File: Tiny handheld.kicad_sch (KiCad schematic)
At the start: 39 parts, among them IC1 BQ21040DBVR, J1 VDisplay/prog1, J2 HDisplay/prog, J3 USB_C_Receptacle_USB2.0, U1 ATtiny85-20P, U2 ATtiny85-20S

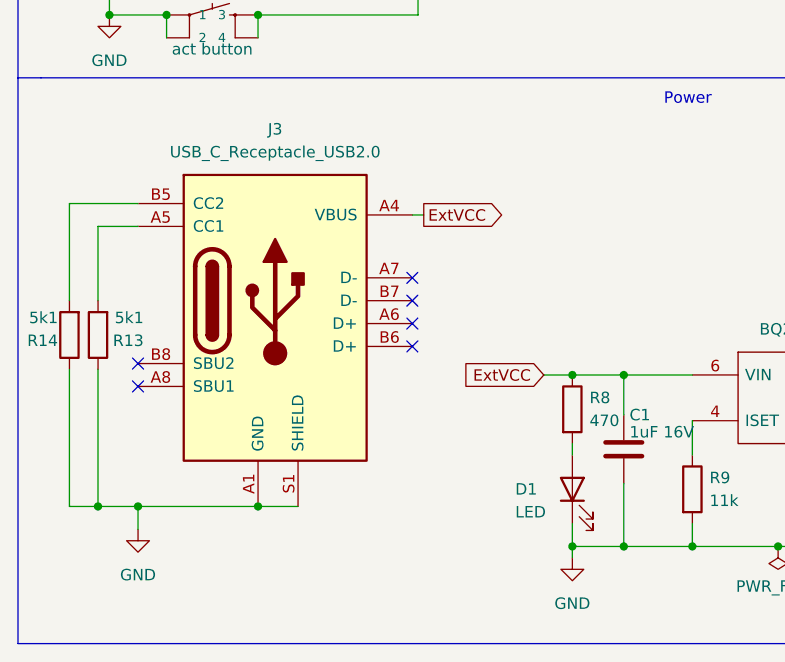
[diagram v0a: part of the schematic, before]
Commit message: added power testpoints
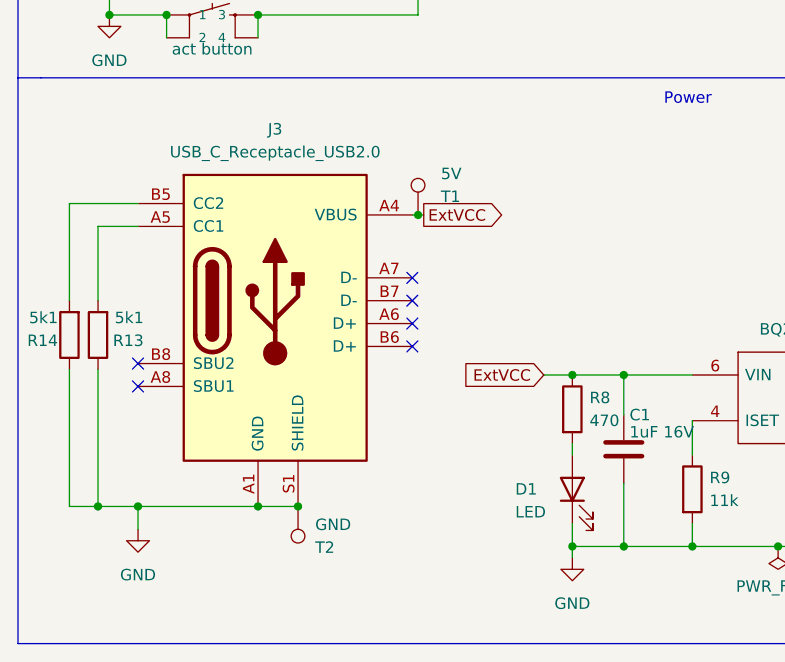
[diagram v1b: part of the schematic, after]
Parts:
- added 5V: T1, TestPoint:TestPoint_Pad_1.0x1.0mm, symbol Connector:TestPoint
- added GND: T2, TestPoint:TestPoint_Pad_1.0x1.0mm, symbol Connector:TestPoint
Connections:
- net ExtVCC: now also 5V.1
- net GND: now also GND.1
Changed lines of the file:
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@@
   (junction (at 117.475 133.985) (diameter 0) (color 0 0 0 0)
   )
+  (junction (at 43.815 137.16) (diameter 0) (color 0 0 0 0)
+  )
   (junction (at 107.315 141.605) (diameter 0) (color 0 0 0 0)
   )
@@
   )
   (junction (at 165.1 29.845) (diameter 0) (color 0 0 0 0)
+  )
+  (junction (at 57.15 104.775) (diameter 0) (color 0 0 0 0)
   )
   (junction (at 241.3 72.39) (diameter 0) (color 0 0 0 0)
@@
     (stroke (width 0) (type default) (color 0 0 0 0))
   )
-  (wire (pts (xy 56.515 104.775) (xy 57.785 104.775))
+  (wire (pts (xy 56.515 104.775) (xy 57.15 104.775))
     (stroke (width 0) (type default) (color 0 0 0 0))
   )
@@
   )
   (wire (pts (xy 165.1 29.845) (xy 177.8 29.845))
+    (stroke (width 0) (type default) (color 0 0 0 0))
+  )
+  (wire (pts (xy 57.15 104.775) (xy 57.785 104.775))
     (stroke (width 0) (type default) (color 0 0 0 0))
   )
@@
     (pin "2")
   )
+  (symbol (lib_id "Connector:TestPoint") (at 57.15 104.775 0) (unit 1)
+    (in_bom yes) (on_board yes) (fields_autoplaced)
+    (property "Reference" "5V" (id 0) (at 59.69 100.2029 0)
+      (effects (font (size 1.27 1.27)) (justify left))
+    )
+    (property "Value" "T1" (id 1) (at 59.69 102.7429 0)
+      (effects (font (size 1.27 1.27)) (justify left))
+    )
+    (property "Footprint" "TestPoint:TestPoint_Pad_1.0x1.0mm" (id 2) (at 62.23 104.775 0)
+      (effects (font (size 1.27 1.27)) hide)
+    )
+    (property "Datasheet" "~" (id 3) (at 62.23 104.775 0)
+      (effects (font (size 1.27 1.27)) hide)
+    )
+    (pin "1")
+  )
   (symbol (lib_id "Device:LED") (at 74.295 135.255 90) (unit 1)
     (in_bom yes) (on_board yes)
@@
     (pin "5")
     (pin "6")
+  )
+  (symbol (lib_id "Connector:TestPoint") (at 43.815 137.16 180) (unit 1)
+    (in_bom yes) (on_board yes) (fields_autoplaced)
+    (property "Reference" "GND" (id 0) (at 45.72 139.1919 0)
+      (effects (font (size 1.27 1.27)) (justify right))
+    )
+    (property "Value" "T2" (id 1) (at 45.72 141.7319 0)
+      (effects (font (size 1.27 1.27)) (justify right))
+    )
+    (property "Footprint" "TestPoint:TestPoint_Pad_1.0x1.0mm" (id 2) (at 38.735 137.16 0)
+      (effects (font (size 1.27 1.27)) hide)
+    )
+    (property "Datasheet" "~" (id 3) (at 38.735 137.16 0)
+      (effects (font (size 1.27 1.27)) hide)
+    )
+    (pin "1")
   )
   (symbol (lib_id "Device:C") (at 150.495 60.325 0) (unit 1)
@@
       (reference "#PWR0114") (unit 1) (value "GNDPWR") (footprint "")
     )
+    (path "/340146ae-1dcd-4cc9-b1a4-794b73097a69"
+      (reference "5V") (unit 1) (value "T1") (footprint "TestPoint:TestPoint_Pad_1.0x1.0mm")
+    )
     (path "/d87d81d6-a9f7-455a-b1d8-8ff0988a0a64"
       (reference "BT1") (unit 1) (value "BATTERY-6.8MM_SMD") (footprint "Battery:BatteryHolder_Keystone_3002_1x2032")
@@
       (reference "D2") (unit 1) (value "LED") (footprint "LED_SMD:LED_1206_3216Metric_Pad1.42x1.75mm_HandSolder")
     )
+    (path "/42350c44-064d-4037-affd-69bc19043671"
+      (reference "GND") (unit 1) (value "T2") (footprint "TestPoint:TestPoint_Pad_1.0x1.0mm")
+    )
     (path "/a18d266d-c0d2-4b00-9a60-ec95f250657b"

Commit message: Start Routing
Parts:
- renumbered 5V to 5V1, GND to GND1
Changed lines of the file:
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@@
   (symbol (lib_id "Connector:TestPoint") (at 57.15 104.775 0) (unit 1)
     (in_bom yes) (on_board yes) (fields_autoplaced)
-    (property "Reference" "5V" (id 0) (at 59.69 100.2029 0)
+    (property "Reference" "5V1" (id 0) (at 59.69 100.2029 0)
       (effects (font (size 1.27 1.27)) (justify left))
     )
@@
   (symbol (lib_id "Connector:TestPoint") (at 43.815 137.16 180) (unit 1)
     (in_bom yes) (on_board yes) (fields_autoplaced)
-    (property "Reference" "GND" (id 0) (at 45.72 139.1919 0)
+    (property "Reference" "GND1" (id 0) (at 45.72 139.1919 0)
       (effects (font (size 1.27 1.27)) (justify right))
     )
@@
     )
     (path "/340146ae-1dcd-4cc9-b1a4-794b73097a69"
-      (reference "5V") (unit 1) (value "T1") (footprint "TestPoint:TestPoint_Pad_1.0x1.0mm")
+      (reference "5V1") (unit 1) (value "T1") (footprint "TestPoint:TestPoint_Pad_1.0x1.0mm")
     )
     (path "/d87d81d6-a9f7-455a-b1d8-8ff0988a0a64"
@@
     )
     (path "/42350c44-064d-4037-affd-69bc19043671"
-      (reference "GND") (unit 1) (value "T2") (footprint "TestPoint:TestPoint_Pad_1.0x1.0mm")
+      (reference "GND1") (unit 1) (value "T2") (footprint "TestPoint:TestPoint_Pad_1.0x1.0mm")
     )
     (path "/a18d266d-c0d2-4b00-9a60-ec95f250657b"

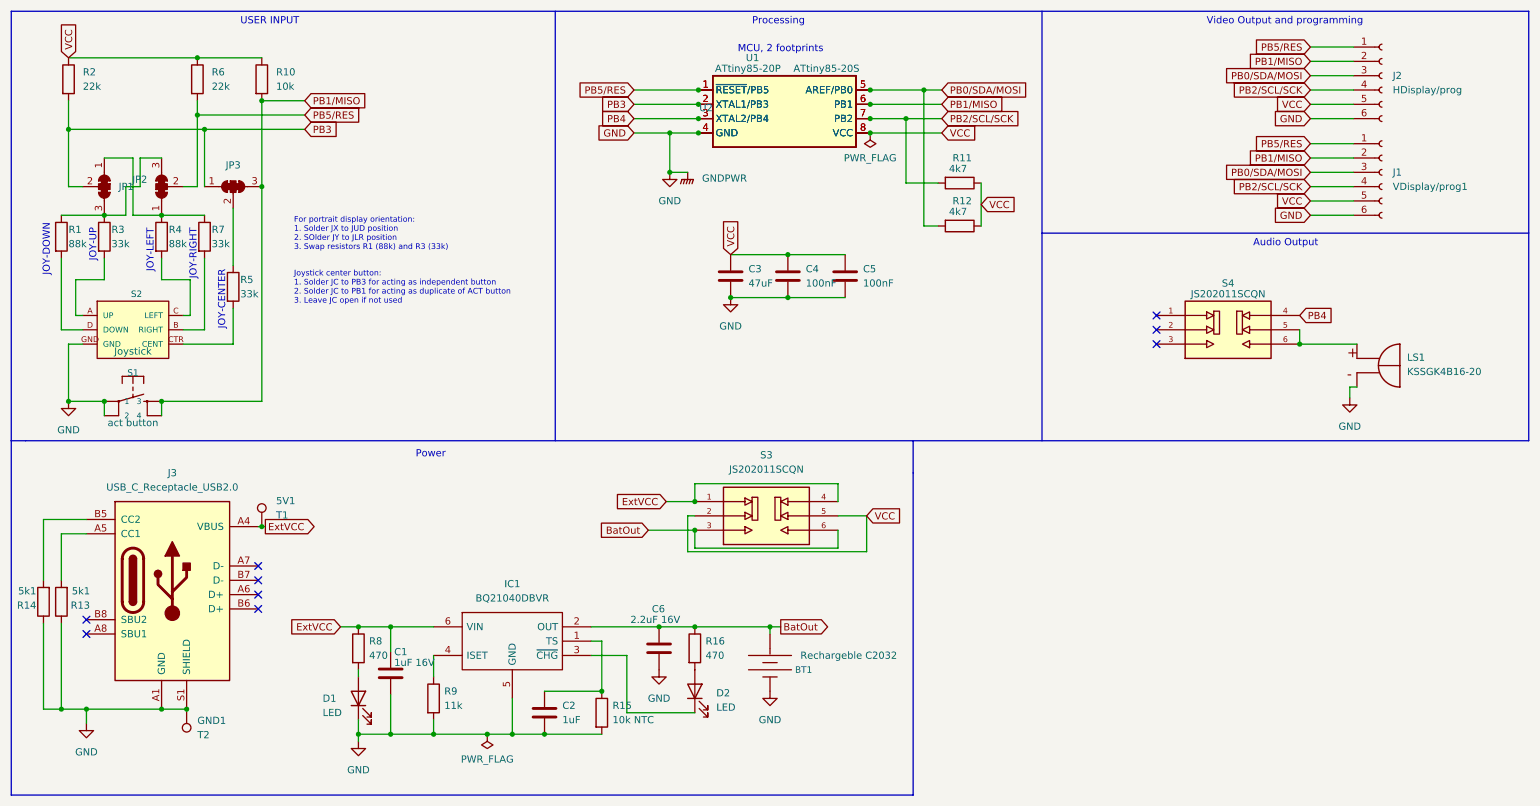
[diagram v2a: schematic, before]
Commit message: enh pcb layout and silkscreen
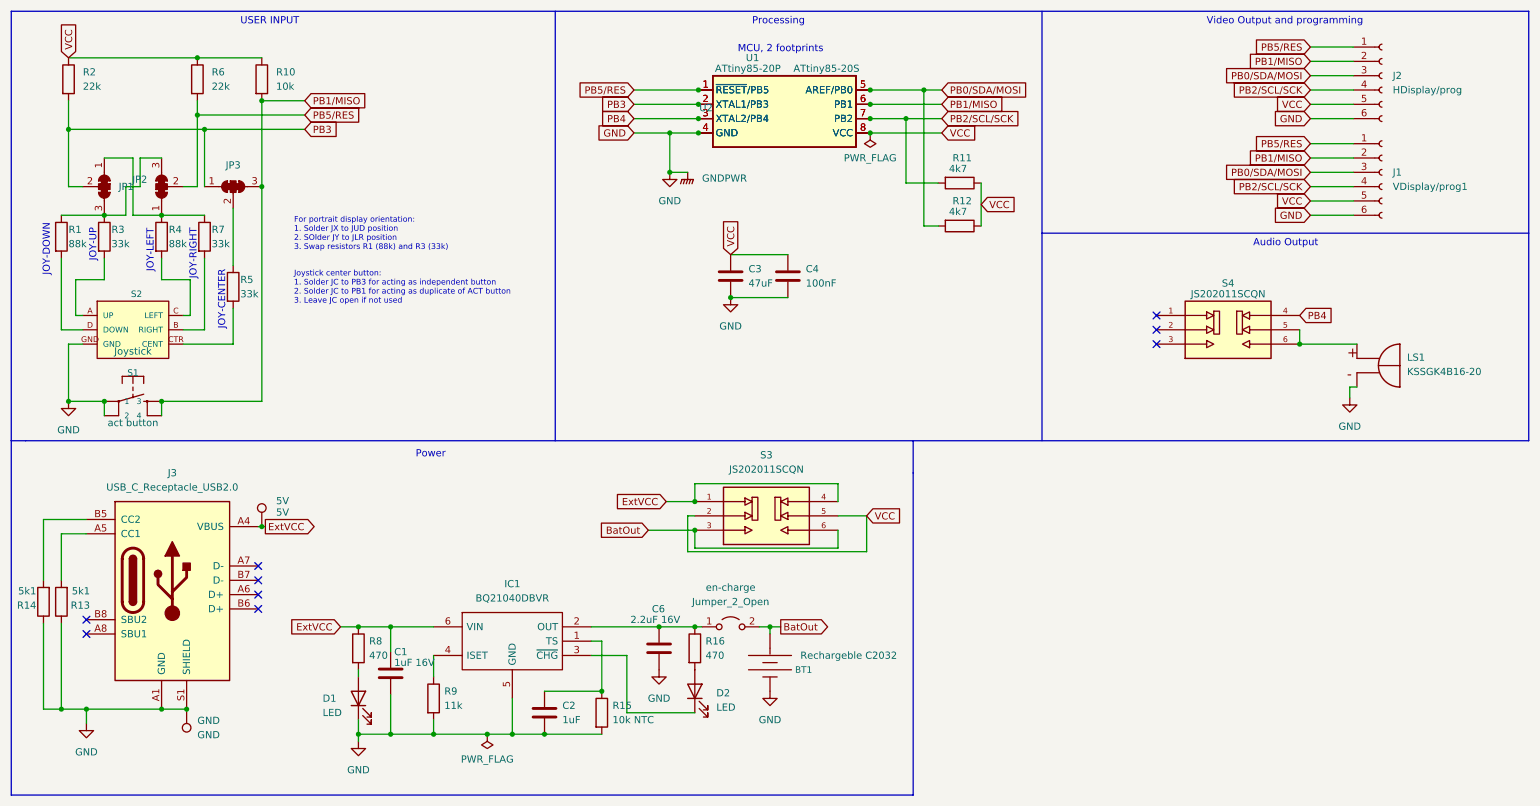
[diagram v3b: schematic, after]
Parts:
- removed C5: 100nF, Capacitor_SMD:C_1206_3216Metric_Pad1.33x1.80mm_HandSolder, symbol Device:C
- added en-charge: Jumper_2_Open, Jumper:SolderJumper-2_P1.3mm_Open_RoundedPad1.0x1.5mm, symbol Jumper:Jumper_2_Open
- 5V: renamed from 5V1; value T1 -> 5V
- GND: renamed from GND1; value T2 -> GND
- R15: Purpose Temperature sense resistor -> Battery temperature sense resistor
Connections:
- net BatOut: now also en-charge.2 (B); no longer C6.1, IC1.2 (OUT), R16.1
- new net: C6.1, IC1.2 (OUT), R16.1, en-charge.1 (A)
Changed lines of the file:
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@@
   (junction (at 80.01 122.555) (diameter 0) (color 0 0 0 0)
   )
+  (junction (at 134.62 32.385) (diameter 0) (color 0 0 0 0)
+  )
+  (junction (at 165.1 34.925) (diameter 0) (color 0 0 0 0)
+  )
+  (junction (at 165.1 32.385) (diameter 0) (color 0 0 0 0)
+  )
+  (junction (at 57.15 44.45) (diameter 0) (color 0 0 0 0)
+  )
+  (junction (at 57.15 29.21) (diameter 0) (color 0 0 0 0)
+  )
+  (junction (at 39.37 137.16) (diameter 0) (color 0 0 0 0)
+  )
+  (junction (at 97.155 141.605) (diameter 0) (color 0 0 0 0)
+  )
+  (junction (at 21.59 137.16) (diameter 0) (color 0 0 0 0)
+  )
+  (junction (at 133.985 100.33) (diameter 0) (color 0 0 0 0)
+  )
+  (junction (at 140.335 64.135) (diameter 0) (color 0 0 0 0)
+  )
+  (junction (at 45.72 21.59) (diameter 0) (color 0 0 0 0)
+  )
+  (junction (at 129.54 41.91) (diameter 0) (color 0 0 0 0)
+  )
+  (junction (at 74.295 141.605) (diameter 0) (color 0 0 0 0)
+  )
+  (junction (at 134.62 34.925) (diameter 0) (color 0 0 0 0)
+  )
+  (junction (at 26.035 137.16) (diameter 0) (color 0 0 0 0)
+  )
+  (junction (at 117.475 133.985) (diameter 0) (color 0 0 0 0)
+  )
+  (junction (at 43.815 137.16) (diameter 0) (color 0 0 0 0)
+  )
+  (junction (at 107.315 141.605) (diameter 0) (color 0 0 0 0)
+  )
+  (junction (at 74.295 122.555) (diameter 0) (color 0 0 0 0)
+  )
+  (junction (at 80.01 141.605) (diameter 0) (color 0 0 0 0)
+  )
+  (junction (at 134.62 27.305) (diameter 0) (color 0 0 0 0)
+  )
+  (junction (at 171.45 32.385) (diameter 0) (color 0 0 0 0)
+  )
+  (junction (at 101.6 141.605) (diameter 0) (color 0 0 0 0)
+  )
+  (junction (at 129.54 34.925) (diameter 0) (color 0 0 0 0)
+  )
   (junction (at 147.32 122.555) (diameter 0) (color 0 0 0 0)
   )
-  (junction (at 134.62 32.385) (diameter 0) (color 0 0 0 0)
-  )
-  (junction (at 165.1 34.925) (diameter 0) (color 0 0 0 0)
-  )
-  (junction (at 165.1 32.385) (diameter 0) (color 0 0 0 0)
-  )
-  (junction (at 57.15 44.45) (diameter 0) (color 0 0 0 0)
-  )
-  (junction (at 57.15 29.21) (diameter 0) (color 0 0 0 0)
-  )
-  (junction (at 39.37 137.16) (diameter 0) (color 0 0 0 0)
-  )
-  (junction (at 97.155 141.605) (diameter 0) (color 0 0 0 0)
-  )
-  (junction (at 21.59 137.16) (diameter 0) (color 0 0 0 0)
-  )
-  (junction (at 133.985 100.33) (diameter 0) (color 0 0 0 0)
-  )
-  (junction (at 140.335 64.135) (diameter 0) (color 0 0 0 0)
-  )
-  (junction (at 45.72 21.59) (diameter 0) (color 0 0 0 0)
-  )
-  (junction (at 129.54 41.91) (diameter 0) (color 0 0 0 0)
-  )
-  (junction (at 74.295 141.605) (diameter 0) (color 0 0 0 0)
-  )
-  (junction (at 134.62 34.925) (diameter 0) (color 0 0 0 0)
-  )
-  (junction (at 26.035 137.16) (diameter 0) (color 0 0 0 0)
-  )
-  (junction (at 117.475 133.985) (diameter 0) (color 0 0 0 0)
-  )
-  (junction (at 43.815 137.16) (diameter 0) (color 0 0 0 0)
-  )
-  (junction (at 107.315 141.605) (diameter 0) (color 0 0 0 0)
-  )
-  (junction (at 74.295 122.555) (diameter 0) (color 0 0 0 0)
-  )
-  (junction (at 80.01 141.605) (diameter 0) (color 0 0 0 0)
-  )
-  (junction (at 134.62 27.305) (diameter 0) (color 0 0 0 0)
-  )
-  (junction (at 171.45 32.385) (diameter 0) (color 0 0 0 0)
-  )
-  (junction (at 101.6 141.605) (diameter 0) (color 0 0 0 0)
-  )
-  (junction (at 129.54 34.925) (diameter 0) (color 0 0 0 0)
-  )
   (junction (at 87.63 141.605) (diameter 0) (color 0 0 0 0)
   )
-  (junction (at 150.495 64.135) (diameter 0) (color 0 0 0 0)
-  )
-  (junction (at 150.495 56.515) (diameter 0) (color 0 0 0 0)
-  )
   (junction (at 22.86 82.55) (diameter 0) (color 0 0 0 0)
   )
   (junction (at 29.21 49.53) (diameter 0) (color 0 0 0 0)
   )
+  (junction (at 46.99 34.29) (diameter 0) (color 0 0 0 0)
+  )
+  (junction (at 165.1 29.845) (diameter 0) (color 0 0 0 0)
+  )
+  (junction (at 57.15 104.775) (diameter 0) (color 0 0 0 0)
+  )
+  (junction (at 241.3 72.39) (diameter 0) (color 0 0 0 0)
+  )
+  (junction (at 133.985 105.41) (diameter 0) (color 0 0 0 0)
+  )
   (junction (at 133.985 122.555) (diameter 0) (color 0 0 0 0)
-  )
-  (junction (at 46.99 34.29) (diameter 0) (color 0 0 0 0)
-  )
-  (junction (at 165.1 29.845) (diameter 0) (color 0 0 0 0)
-  )
-  (junction (at 57.15 104.775) (diameter 0) (color 0 0 0 0)
-  )
-  (junction (at 241.3 72.39) (diameter 0) (color 0 0 0 0)
-  )
-  (junction (at 133.985 105.41) (diameter 0) (color 0 0 0 0)
   )
   (junction (at 39.37 49.53) (diameter 0) (color 0 0 0 0)
@@
     (stroke (width 0) (type default) (color 0 0 0 0))
   )
-  (wire (pts (xy 150.495 64.135) (xy 160.655 64.135))
-    (stroke (width 0) (type default) (color 0 0 0 0))
-  )
   (polyline (pts (xy 109.22 13.335) (xy 109.22 89.535))
     (stroke (width 0) (type default) (color 0 0 0 0))
@@
     (stroke (width 0) (type default) (color 0 0 0 0))
   )
-  (wire (pts (xy 150.495 56.515) (xy 160.655 56.515))
-    (stroke (width 0) (type default) (color 0 0 0 0))
-  )
   (wire (pts (xy 87.63 141.605) (xy 97.155 141.605))
     (stroke (width 0) (type default) (color 0 0 0 0))
@@
     (stroke (width 0) (type default) (color 0 0 0 0))
   )
+  (wire (pts (xy 145.415 122.555) (xy 147.32 122.555))
+    (stroke (width 0) (type default) (color 0 0 0 0))
+  )
   (wire (pts (xy 241.3 72.39) (xy 251.46 72.39))
     (stroke (width 0) (type default) (color 0 0 0 0))
@@
     (stroke (width 0) (type default) (color 0 0 0 0))
   )
+  (wire (pts (xy 133.985 122.555) (xy 135.255 122.555))
+    (stroke (width 0) (type default) (color 0 0 0 0))
+  )
   (wire (pts (xy 121.92 137.795) (xy 121.92 127.635))
     (stroke (width 0) (type default) (color 0 0 0 0))
@@
   )
   (polyline (pts (xy 281.94 13.335) (xy 12.7 13.335))
-    (stroke (width 0) (type default) (color 0 0 0 0))
-  )
-  (wire (pts (xy 133.985 122.555) (xy 147.32 122.555))
     (stroke (width 0) (type default) (color 0 0 0 0))
   )
@@
   )
   (symbol (lib_id "Connector:TestPoint") (at 57.15 104.775 0) (unit 1)
-    (in_bom yes) (on_board yes) (fields_autoplaced)
-    (property "Reference" "5V1" (id 0) (at 59.69 100.2029 0)
-      (effects (font (size 1.27 1.27)) (justify left))
-    )
-    (property "Value" "T1" (id 1) (at 59.69 102.7429 0)
+    (in_bom yes) (on_board yes)
+    (property "Reference" "5V" (id 0) (at 59.69 100.2029 0)
+      (effects (font (size 1.27 1.27)) (justify left))
+    )
+    (property "Value" "5V" (id 1) (at 59.69 102.235 0)
       (effects (font (size 1.27 1.27)) (justify left))
     )
@@
   (symbol (lib_id "Connector:TestPoint") (at 43.815 137.16 180) (unit 1)
     (in_bom yes) (on_board yes) (fields_autoplaced)
-    (property "Reference" "GND1" (id 0) (at 45.72 139.1919 0)
+    (property "Reference" "GND" (id 0) (at 45.72 139.1919 0)
       (effects (font (size 1.27 1.27)) (justify right))
     )
-    (property "Value" "T2" (id 1) (at 45.72 141.7319 0)
+    (property "Value" "GND" (id 1) (at 45.72 141.7319 0)
       (effects (font (size 1.27 1.27)) (justify right))
     )
@@
     (pin "2")
   )
-  (symbol (lib_id "Device:C") (at 160.655 60.325 0) (unit 1)
-    (in_bom yes) (on_board yes) (fields_autoplaced)
-    (property "Reference" "C5" (id 0) (at 163.83 59.0549 0)
-      (effects (font (size 1.27 1.27)) (justify left))
-    )
-    (property "Value" "100nF" (id 1) (at 163.83 61.5949 0)
-      (effects (font (size 1.27 1.27)) (justify left))
-    )
-    (property "Footprint" "Capacitor_SMD:C_1206_3216Metric_Pad1.33x1.80mm_HandSolder" (id 2) (at 161.6202 64.135 0)
-      (effects (font (size 1.27 1.27)) hide)
-    )
-    (property "Datasheet" "~" (id 3) (at 160.655 60.325 0)
+  (symbol (lib_id "Jumper:Jumper_2_Open") (at 140.335 122.555 0) (unit 1)
+    (in_bom yes) (on_board yes) (fields_autoplaced)
+    (property "Reference" "en-charge" (id 0) (at 140.335 115.57 0))
+    (property "Value" "Jumper_2_Open" (id 1) (at 140.335 118.11 0))
+    (property "Footprint" "Jumper:SolderJumper-2_P1.3mm_Open_RoundedPad1.0x1.5mm" (id 2) (at 140.335 122.555 0)
+      (effects (font (size 1.27 1.27)) hide)
+    )
+    (property "Datasheet" "~" (id 3) (at 140.335 122.555 0)
       (effects (font (size 1.27 1.27)) hide)
     )
@@
       (effects (font (size 1.27 1.27)) hide)
     )
-    (property "Purpose" "Temperature sense resistor" (id 4) (at 117.475 137.795 0)
+    (property "Purpose" "Battery temperature sense resistor" (id 4) (at 117.475 137.795 0)
       (effects (font (size 1.27 1.27)) hide)
     )
@@
     )
     (path "/340146ae-1dcd-4cc9-b1a4-794b73097a69"
-      (reference "5V1") (unit 1) (value "T1") (footprint "TestPoint:TestPoint_Pad_1.0x1.0mm")
+      (reference "5V") (unit 1) (value "5V") (footprint "TestPoint:TestPoint_Pad_1.0x1.0mm")
     )
     (path "/d87d81d6-a9f7-455a-b1d8-8ff0988a0a64"
@@
       (reference "C4") (unit 1) (value "100nF") (footprint "Capacitor_SMD:C_1206_3216Metric_Pad1.33x1.80mm_HandSolder")
     )
-    (path "/b73c30b1-4672-42e9-a953-ea6ea6d080fb"
-      (reference "C5") (unit 1) (value "100nF") (footprint "Capacitor_SMD:C_1206_3216Metric_Pad1.33x1.80mm_HandSolder")
-    )
     (path "/322f80a4-589e-4a0d-a6c6-3cc8a238e65a"
       (reference "C6") (unit 1) (value "2.2uF 16V") (footprint "Capacitor_SMD:C_1206_3216Metric_Pad1.33x1.80mm_HandSolder")
@@
     )
     (path "/42350c44-064d-4037-affd-69bc19043671"
-      (reference "GND1") (unit 1) (value "T2") (footprint "TestPoint:TestPoint_Pad_1.0x1.0mm")
+      (reference "GND") (unit 1) (value "GND") (footprint "TestPoint:TestPoint_Pad_1.0x1.0mm")
     )
     (path "/a18d266d-c0d2-4b00-9a60-ec95f250657b"
@@
       (reference "U2") (unit 1) (value "ATtiny85-20S") (footprint "Package_SO:SOIC-8W_5.3x5.3mm_P1.27mm")
     )
-  )
+    (path "/bc823d2e-cd93-4e16-8824-0c0bbb02b3b1"
+      (reference "en-charge") (unit 1) (value "Jumper_2_Open") (footprint "Jumper:SolderJumper-2_P1.3mm_Open_RoundedPad1.0x1.5mm")
+    )
+  )
